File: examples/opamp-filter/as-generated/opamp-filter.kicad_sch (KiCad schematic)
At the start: 19 parts, among them J1 IN, J2 5V, J3 OUT, U1 MCP6001R, U2 MCP6001R

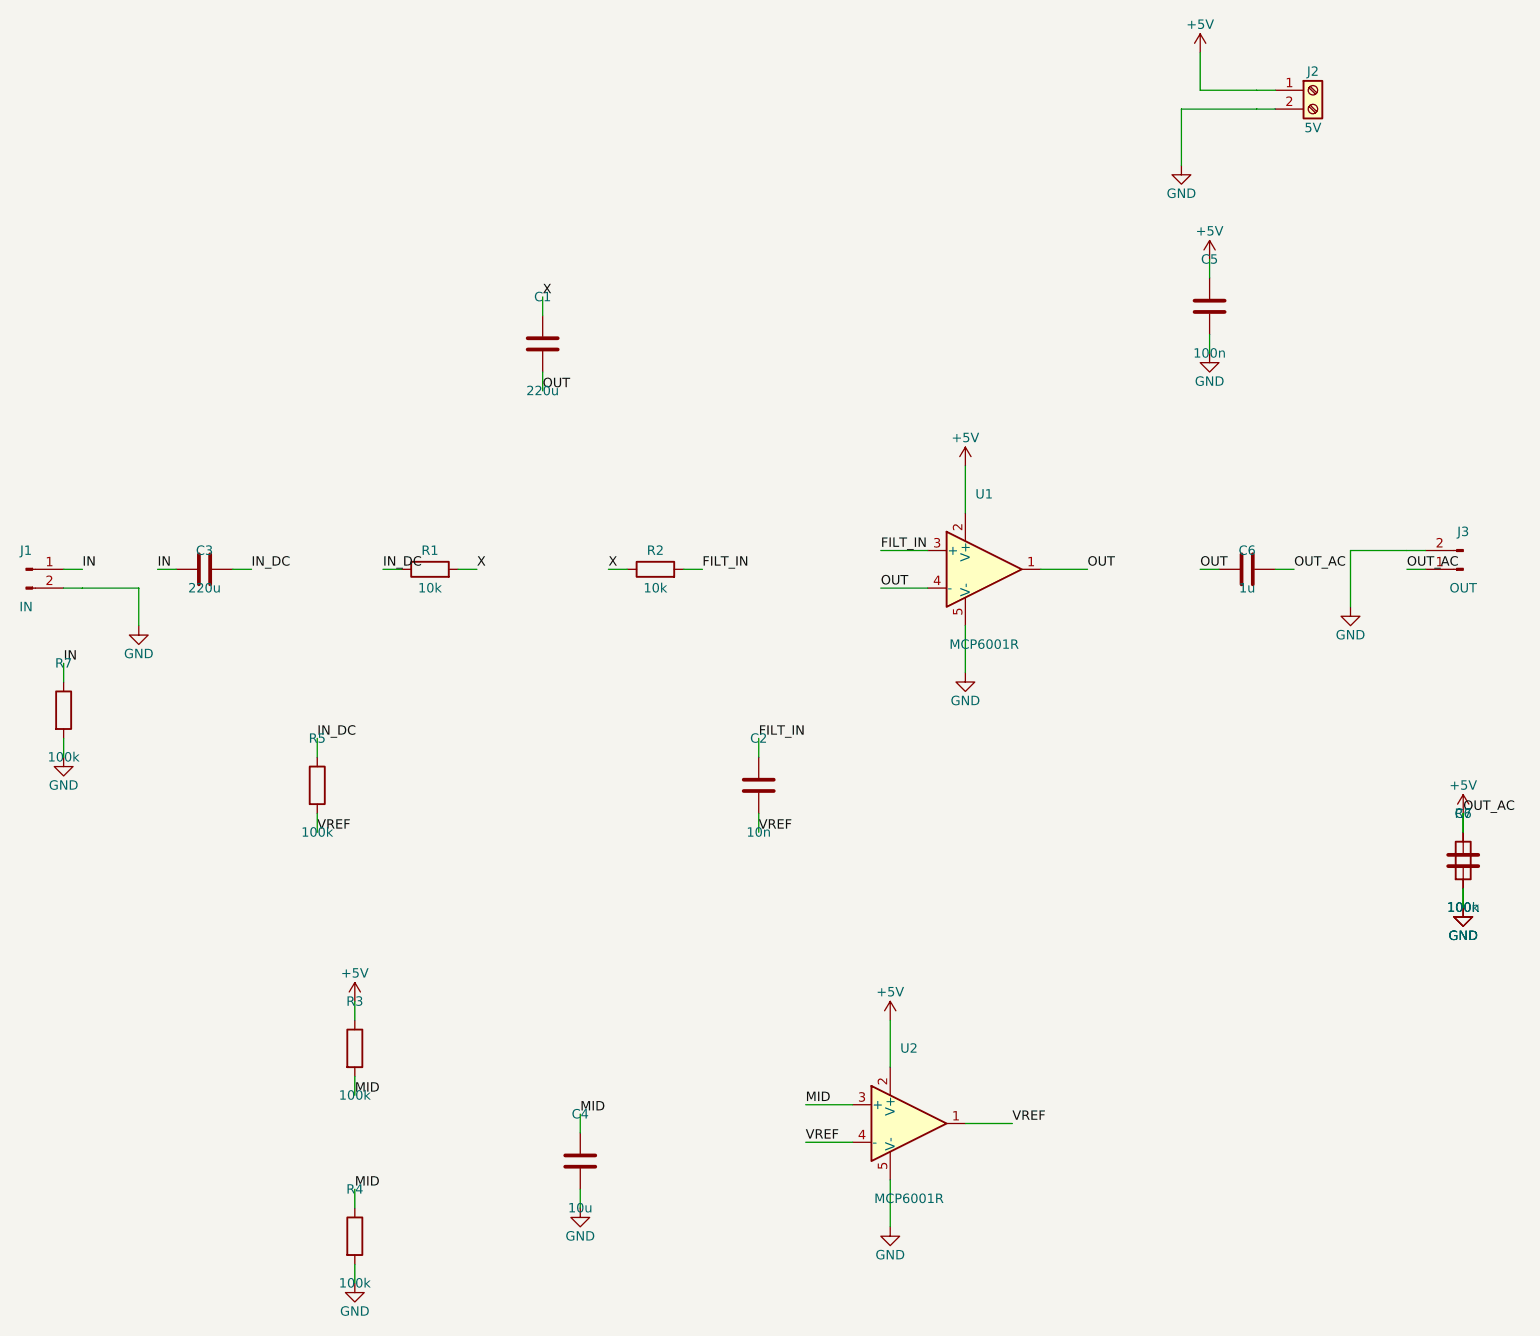
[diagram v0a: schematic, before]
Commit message: Regenerate the five as round three drew them
All five reviewed projects pass their gates again: the buck all wire
with its feedback drawn home, the motor's logic named at the header,
the carrier reading as the pinout table it is - with its feed diode
finally pointing the right way - the filter compact with test points,
and the FPGA's capacitors sitting beside the units they feed. Thirty
renders redrawn, verdict tables at today's numbers.

Co-Authored-By: Claude Fable 5 <noreply@anthropic.com>
Claude-Session: https://claude.ai/code/session_01DUj7Ltu92tWg159mCSacwY
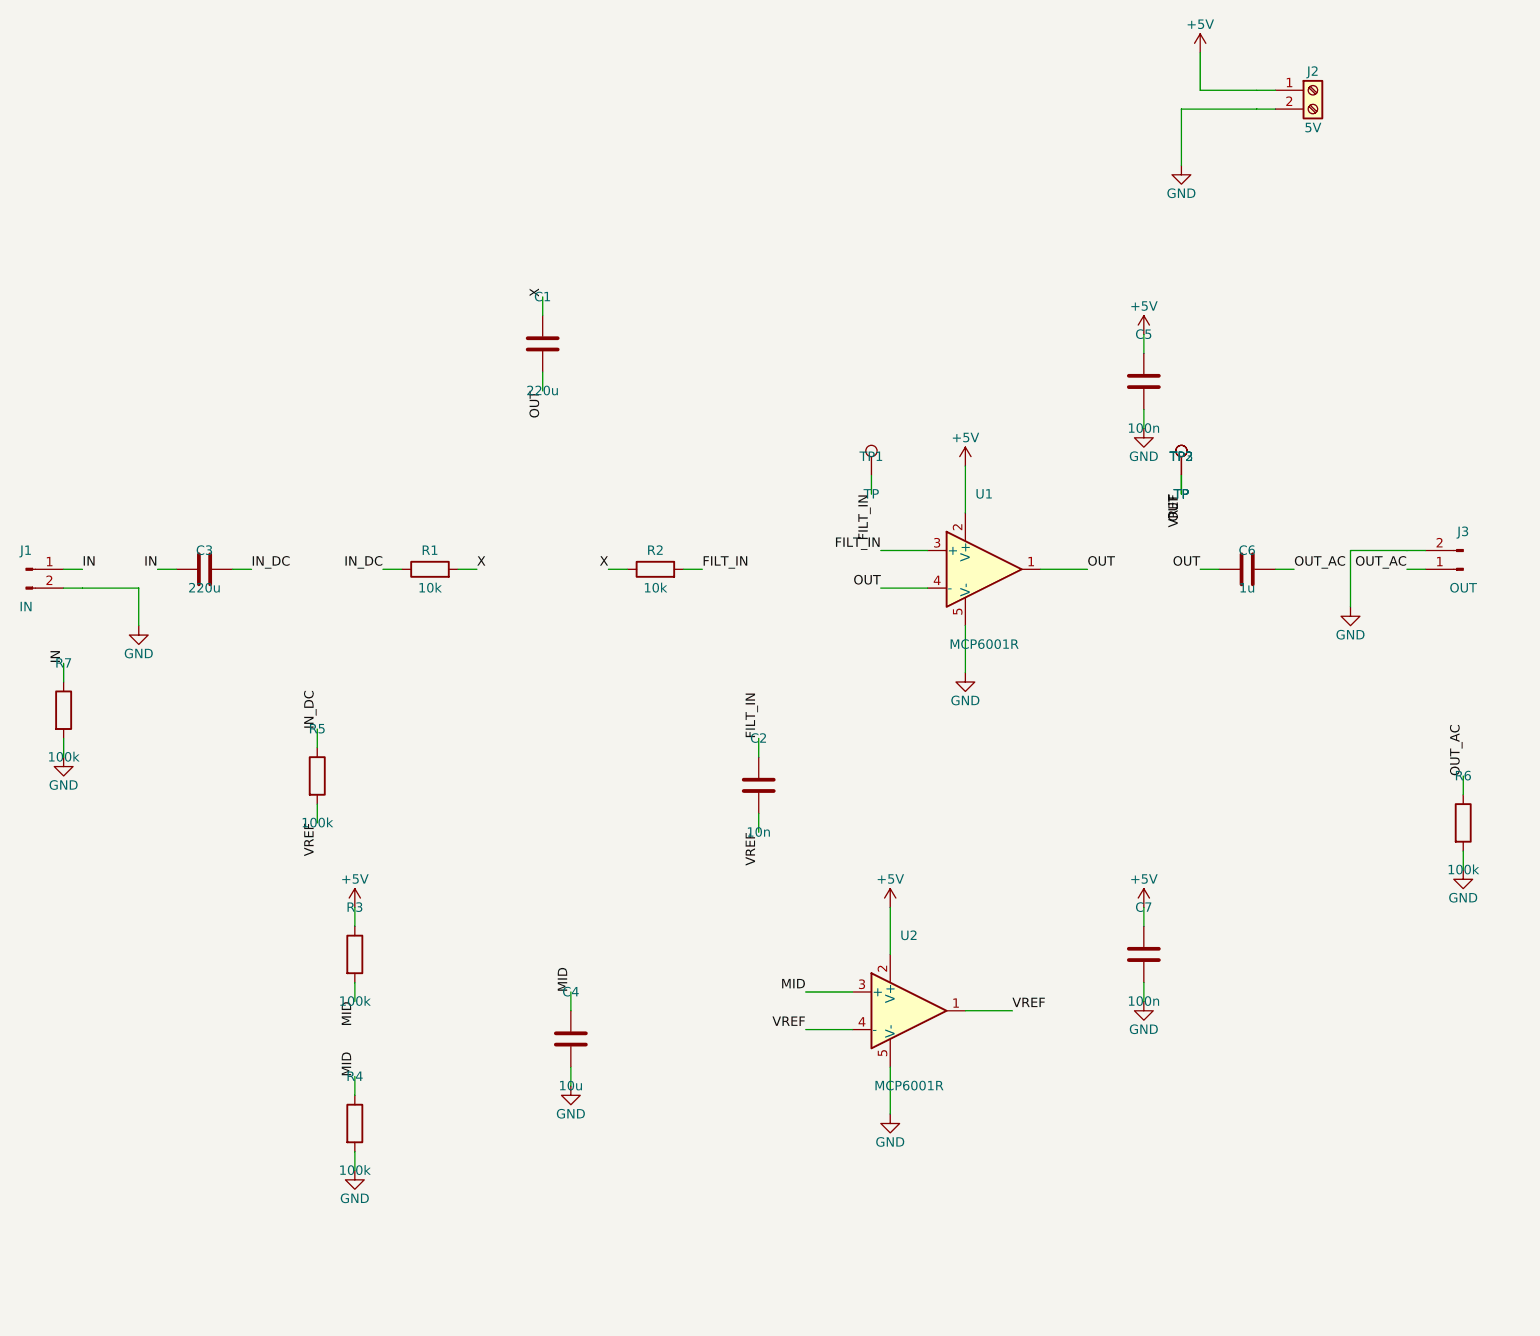
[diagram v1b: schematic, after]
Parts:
- added TP1, TP2, TP3: TP, TestPoint:TestPoint_Pad_D1.5mm, symbol Connector:TestPoint
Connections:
- net VREF is gone; now on net OUT: C2.2, R5.2, U2.1, U2.4 (-)
- net +5V: no longer C6.2, J3.1 (Pin_1), R6.1
- net FILT_IN: now also TP1.1
- net OUT: now also TP2.1, TP3.1
- new net OUT_AC: C6.2, J3.1 (Pin_1), R6.1
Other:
- moved on the sheet: C4, C5, C7, R3, R4, R5, R6, U2

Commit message: Regenerate the four the text and width work changed
Designators and values off the rails they were printed on, power-named
nets at the width their rule asks for, and the buck's feedback ending
on the capacitor pad it senses at.

Co-Authored-By: Claude Fable 5 <noreply@anthropic.com>
Claude-Session: https://claude.ai/code/session_01DUj7Ltu92tWg159mCSacwY
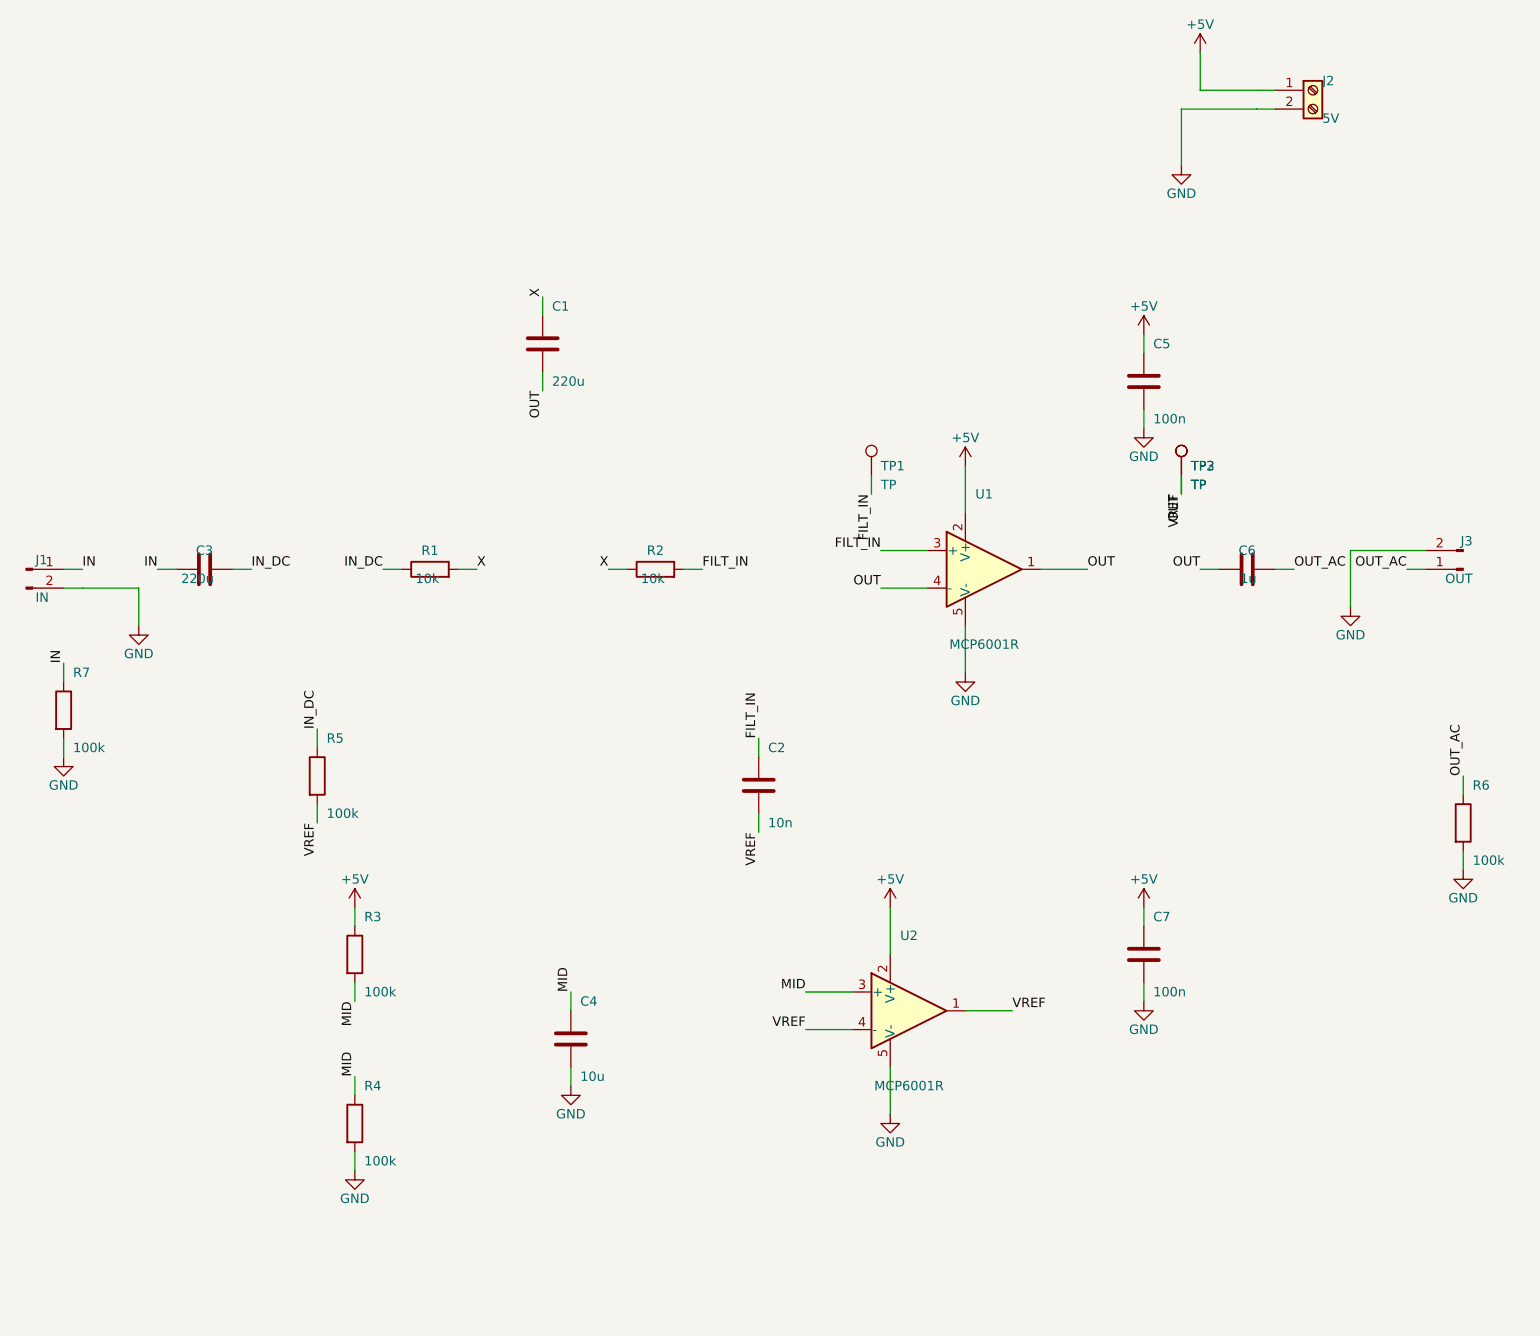
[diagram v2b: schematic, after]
